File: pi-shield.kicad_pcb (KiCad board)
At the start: 2 copper layers, 65 x 56 mm, 34 parts, among them J1 Conn_02x20_Odd_Even, J10 Conn_01x04, J2 Conn_01x04, J3 Conn_01x04, J4 0530470210, J5 Conn_01x05, J6 Conn_01x07, J7 0530471410, J8 Conn_01x04, J9 Conn_01x04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

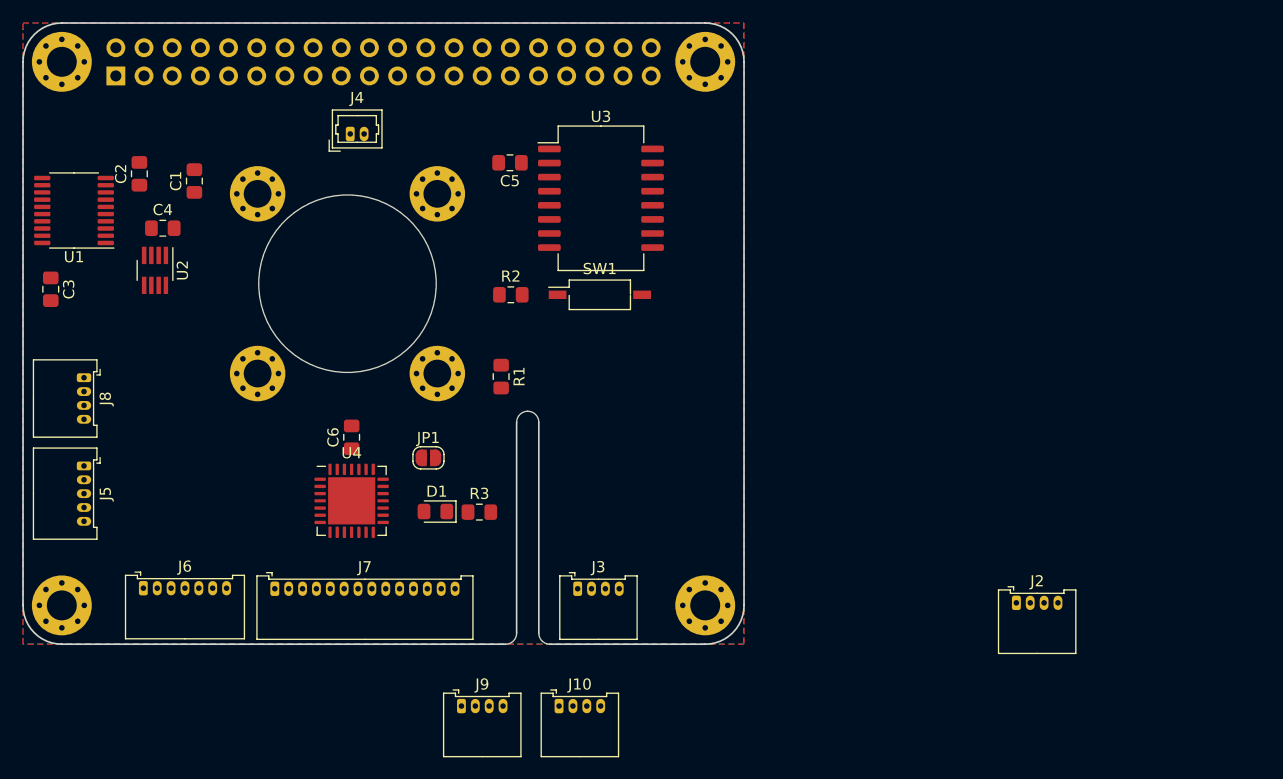
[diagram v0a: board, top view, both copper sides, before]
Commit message: Progress on schematic and board outline
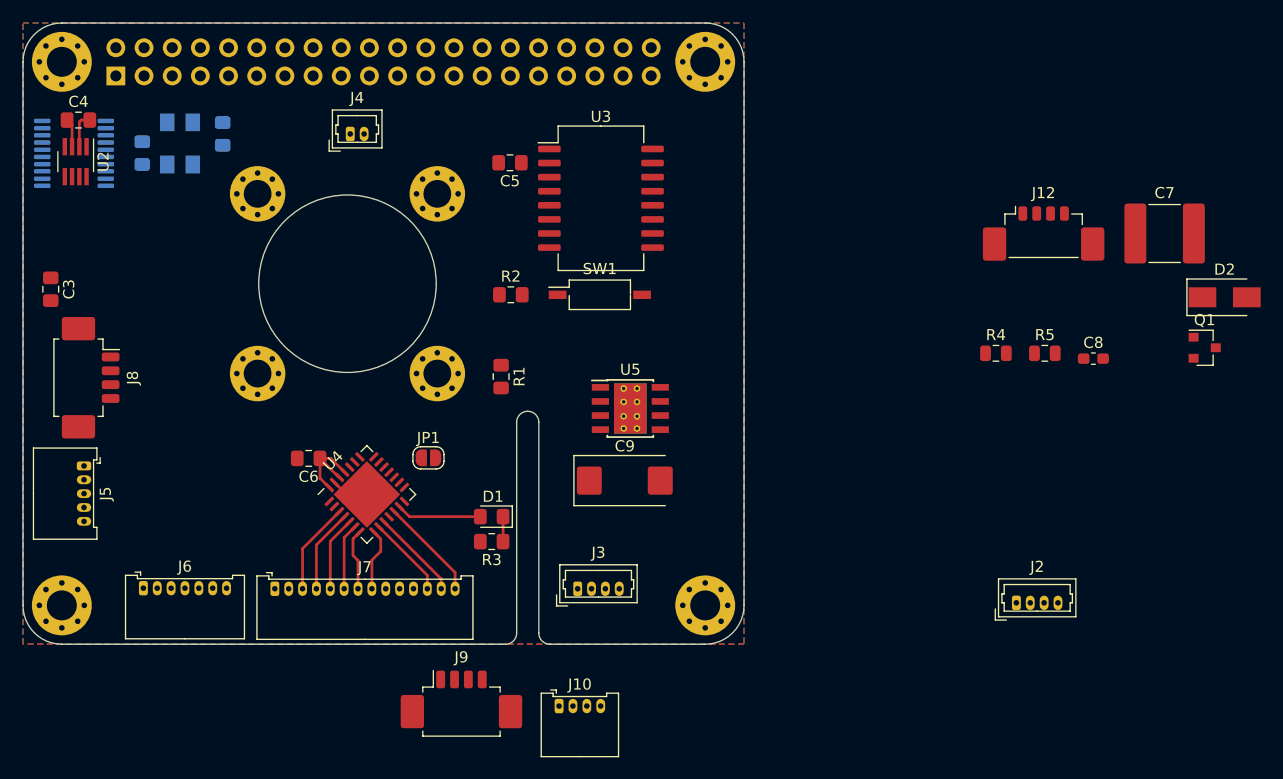
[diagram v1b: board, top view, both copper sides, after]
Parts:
- added C7: 10u, Capacitor_SMD:C_2220_5650Metric_Pad1.97x5.40mm_HandSolder, F.Cu at (139.4, 55.5)
- added C8: 10n, Capacitor_SMD:C_0603_1608Metric_Pad1.05x0.95mm_HandSolder, F.Cu at (133.0, 66.8)
- added C9: 330u, Capacitor_Tantalum_SMD:CP_EIA-7343-30_AVX-N_Pad2.25x2.55mm_HandSolder, F.Cu at (90.8, 77.8)
- added D2: B340A, Diode_SMD:D_SMA, F.Cu at (144.8, 61.2)
- added J12: Conn_01x03, Connector_Molex:Molex_PicoBlade_53398-0471_1x04-1MP_P1.25mm_Vertical, F.Cu at (128.5, 54.9)
- added Q1: DMP3099L, Package_TO_SOT_SMD:SOT-23, F.Cu at (143.0, 65.8)
- added R4: 10k, Resistor_SMD:R_0805_2012Metric, F.Cu at (124.2, 66.3)
- added R5: 3k24, Resistor_SMD:R_0805_2012Metric, F.Cu at (128.6, 66.3)
- added U5: TPS5430DDA, Package_SO:TI_SO-PowerPAD-8_ThermalVias, F.Cu at (91.2, 71.2)
- added Y1: 20Mhz, Crystal:Crystal_SMD_Abracon_ABM3C-4Pin_5.0x3.2mm, B.Cu at (50.6, 47.4)
- C1, C2, U1: moved to B.Cu
- J2, J3: footprint Connector_Molex:Molex_PicoBlade_53048-0410_1x04_P1.25mm_Horizontal -> Connector_Molex:Molex_PicoBlade_53047-0410_1x04_P1.25mm_Vertical
- J8, J9: footprint Connector_Molex:Molex_PicoBlade_53048-0410_1x04_P1.25mm_Horizontal -> Connector_Molex:Molex_PicoBlade_53261-0471_1x04-1MP_P1.25mm_Horizontal
- moved C4 12.4 mm to (41.5, 45.2)
- moved U2 12.1 mm to (41.2, 49.0)
- moved U1 5.15 mm to (41.1, 48.2)
- moved D1 5.10 mm to (78.8, 81.0)
- moved C1 4.95 mm to (54.5, 46.5), turned to 270 degrees
- moved C6 4.32 mm to (62.2, 75.8), turned to 180 degrees
- moved R3 2.88 mm to (78.8, 83.2), turned to 180 degrees
- moved C2 1.89 mm to (47.2, 48.2)
- moved U4 1.49 mm to (67.5, 79.0), turned to 45 degrees
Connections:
- J1 pad 1: Net-(J1-Pad1) -> +3V3
- J1 pad 36: Net-(J1-Pad36) -> /VBUS_DIS
- J1 pad 37: Net-(J1-Pad37) -> /CAN_INT
- U4 pad 13: Net-(U4-Pad13) -> /LED_BOARD
- U4 pad 16: /LED_BOARD -> Net-(U4-Pad16)
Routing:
- net +3V3: track 0.00 -> 10.8 mm
- net /LED_RGB_B: track 0.00 -> 9.22 mm
- net /LED_READY: track 0.00 -> 8.33 mm
- net /LED_RGB_G: track 0.00 -> 8.17 mm
- net /LED_BOARD: track 0.00 -> 7.68 mm
- net /LED_DEBUG: track 0.00 -> 7.55 mm
- net /LED_RGB_R: track 0.00 -> 7.38 mm
- net /LED_BUS: track 0.00 -> 6.76 mm
- net GND: track 0.00 -> 6.62 mm
- net /LED_COMM: track 0.00 -> 5.97 mm
- net /LED_POWER: track 0.00 -> 5.70 mm
- net /LED_ERROR: track 0.00 -> 5.56 mm
- net Net-(D1-Pad1): track 0.00 -> 2.25 mm

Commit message: Initial component placement
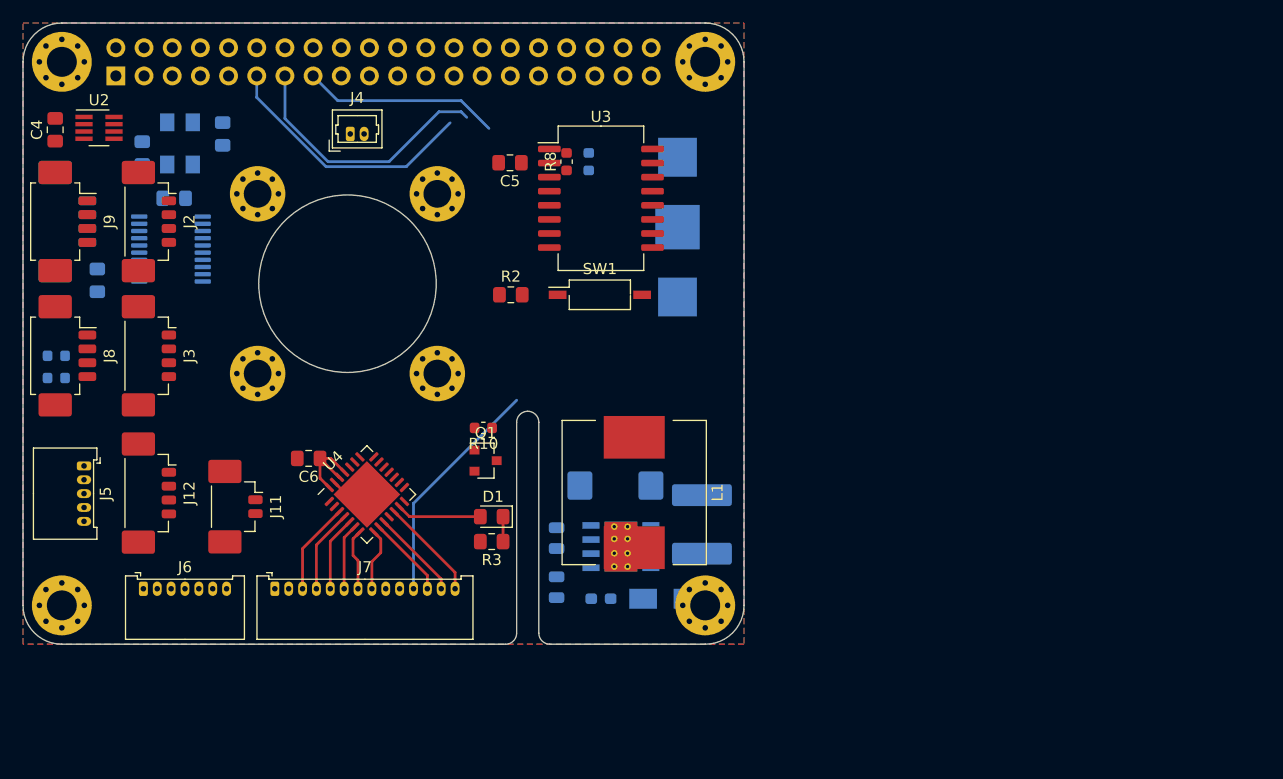
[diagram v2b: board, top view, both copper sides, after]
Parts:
- removed JP1: Jumper_NO_Small, Jumper:SolderJumper-2_P1.3mm_Open_RoundedPad1.0x1.5mm
- added BT1: 3V, pi-shield:3030, B.Cu at (95.5, 54.9)
- added J11: 0530470210, Connector_Molex:Molex_PicoBlade_53398-0271_1x02-1MP_P1.25mm_Vertical, F.Cu at (56.2, 80.1)
- added L1: 33uH, pi-shield:DR127, F.Cu at (91.6, 78.8)
- added R10: 10k, Resistor_SMD:R_0603_1608Metric, F.Cu at (78.0, 73.0)
- added R6: 100, Resistor_SMD:R_0603_1608Metric, B.Cu at (39.5, 66.5)
- added R7: 100, Resistor_SMD:R_0603_1608Metric, B.Cu at (39.5, 68.5)
- added R8: 1k, Resistor_SMD:R_0603_1608Metric, F.Cu at (85.5, 49.0)
- added R9: 1k, Resistor_SMD:R_0603_1608Metric, B.Cu at (87.5, 49.0)
- C3, C7, C8, C9, D2, R1, R4, R5, U5: moved to B.Cu
- J10: footprint Connector_Molex:Molex_PicoBlade_53048-0410_1x04_P1.25mm_Horizontal -> Connector_Molex:Molex_PicoBlade_53261-0471_1x04-1MP_P1.25mm_Horizontal; moved to B.Cu
- J2, J3: footprint Connector_Molex:Molex_PicoBlade_53047-0410_1x04_P1.25mm_Vertical -> Connector_Molex:Molex_PicoBlade_53398-0471_1x04-1MP_P1.25mm_Vertical
- moved J2 84.9 mm to (48.4, 54.4), turned to 270 degrees
- moved J12 83.6 mm to (48.4, 78.9), turned to 270 degrees
- moved Q1 65.6 mm to (78.2, 76.0)
- moved J10 62.7 mm to (39.9, 54.4), turned to 90 degrees
- moved D2 57.3 mm to (94.4, 88.4)
- moved J9 56.7 mm to (39.9, 54.4), turned to 270 degrees
- moved C8 49.4 mm to (88.6, 88.4), turned to 180 degrees
- moved C7 49.3 mm to (97.7, 81.7), turned to 90 degrees
- moved R5 48.8 mm to (84.6, 87.4), turned to 270 degrees
- moved J3 43.5 mm to (48.4, 66.5), turned to 270 degrees
- moved R4 43.0 mm to (84.6, 82.9), turned to 270 degrees
- moved R1 37.4 mm to (43.2, 59.7), turned to 90 degrees
- moved C3 13.8 mm to (50.1, 52.3), turned to 0 degrees
- moved U5 12.5 mm to (90.4, 83.7)
- moved U1 12.3 mm to (49.8, 56.9)
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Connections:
- J1 pad 10: /UART_RX -> Net-(J1-Pad10)
- J1 pad 32: Net-(J1-Pad32) -> /ROBOT_SELECT
- J1 pad 8: /UART_TX -> Net-(J1-Pad8)
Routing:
- net /BTN_START: track 0.00 -> 38.7 mm
- net /BTN_TEAM2: track 0.00 -> 23.9 mm
- net /BTN_TEAM1: track 0.00 -> 23.6 mm
- net GND: track 6.62 -> 3.38 mm
- net +3V3: track 10.8 -> 8.17 mm
- added copper zone on In1.Cu, net GND
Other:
- copper layers 2 -> 4

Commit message: Made some progress with layout
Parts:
- R1, R2, R3: footprint Resistor_SMD:R_0805_2012Metric_Pad1.15x1.40mm_HandSolder -> Resistor_SMD:R_0603_1608Metric
- R4, R5: footprint Resistor_SMD:R_0805_2012Metric -> Resistor_SMD:R_0603_1608Metric; moved to F.Cu
- R8: moved to B.Cu
- moved C1 28.6 mm to (43.8, 73.0), turned to 180 degrees
- moved Y1 26.6 mm to (48.5, 73.8), turned to 90 degrees
- moved C2 25.3 mm to (52.2, 73.0), turned to 270 degrees
- moved J4 24.8 mm to (80.6, 66.5), turned to 90 degrees
- moved C3 11.8 mm to (44.2, 62.5), turned to 90 degrees
- moved U1 9.64 mm to (49.2, 66.5)
- moved C4 7.31 mm to (46.7, 45.7), turned to 270 degrees
- moved R1 5.96 mm to (42.9, 65.7), turned to 0 degrees
- moved R8 4.34 mm to (88.9, 51.7), turned to 180 degrees
- moved D2 4.30 mm to (90.1, 88.5), turned to 180 degrees
- moved C8 4.28 mm to (84.4, 87.6), turned to 90 degrees
- moved R5 4.07 mm to (84.3, 83.3)
- moved R7 3.61 mm to (39.8, 64.9), turned to 90 degrees
- moved R4 3.40 mm to (84.3, 79.5)
- moved R6 2.03 mm to (38.2, 64.9), turned to 90 degrees
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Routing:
- net /TS_INT: track 0.00 -> 131.2 mm
- net +5V: track 0.00 -> 127.6 mm, vias 0 -> 4
- net /SDA: track 0.00 -> 119.9 mm, vias 0 -> 4
- net /SCL: track 0.00 -> 115.6 mm, vias 0 -> 3
- net /SCLK: track 0.00 -> 76.3 mm, vias 0 -> 1
- net +12V: track 0.00 -> 74.2 mm, vias 0 -> 2
- net /MOSI: track 0.00 -> 70.4 mm, vias 0 -> 2
- net /SHDN_OK: track 0.00 -> 69.9 mm, vias 0 -> 2
- net /CS1: track 0.00 -> 68.5 mm
- net /SHDN_REQ: track 0.00 -> 67.2 mm, vias 0 -> 2
- net /CAN_INT: track 0.00 -> 65.1 mm
- net /LCD_RST: track 0.00 -> 64.9 mm, vias 0 -> 2
- net /LCD_RS: track 0.00 -> 58.8 mm, vias 0 -> 2
- net /CS0: track 0.00 -> 46.7 mm, vias 0 -> 1
- net /CANL: track 0.00 -> 45.4 mm, vias 0 -> 1
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- added copper zone on In2.Cu, net +3V3
- added copper zone on B.Cu, net +5V
- added copper zone on F.Cu, net +5V

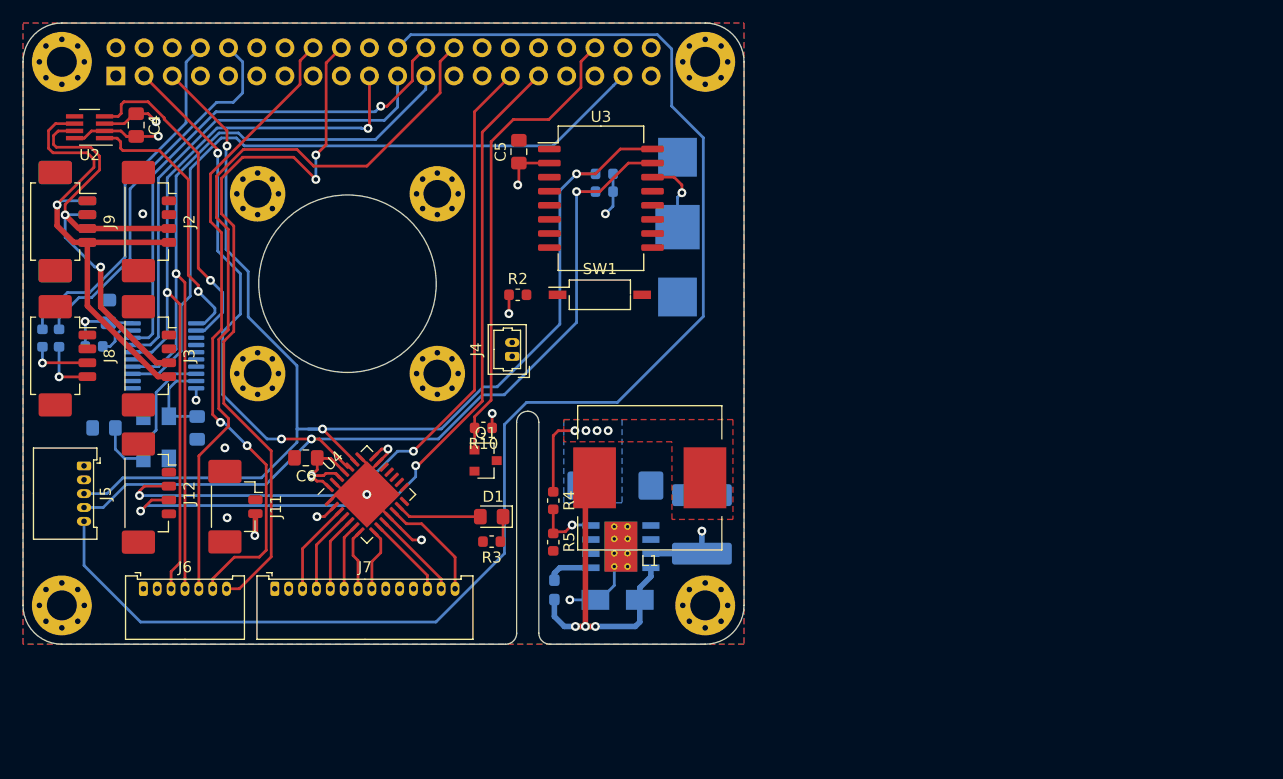
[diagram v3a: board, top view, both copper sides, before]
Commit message: First complete layout
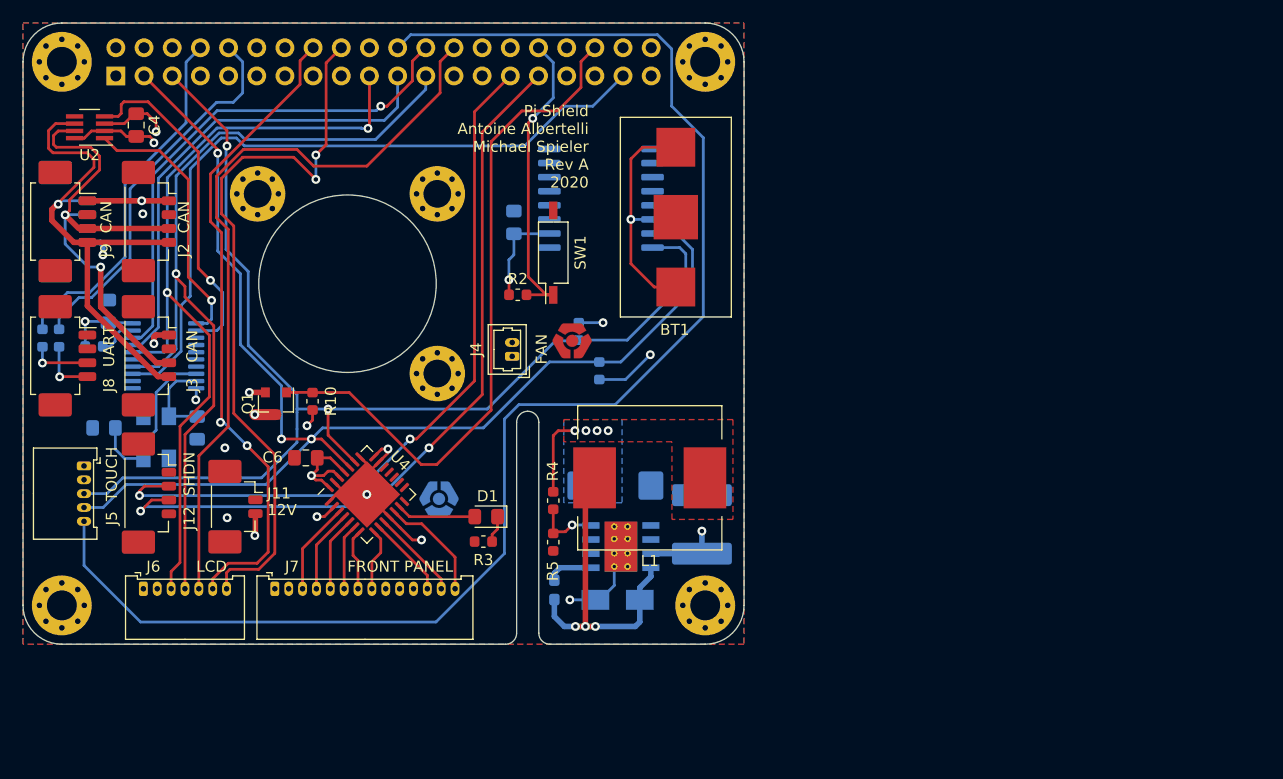
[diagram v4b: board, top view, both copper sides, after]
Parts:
- removed H4: M2, MountingHole:MountingHole_2.5mm_Pad_Via
- added G***: LOGO, pi-shield:CVRA-logo-small-copper, B.Cu at (74.0, 79.4)
- added G***: LOGO, pi-shield:CVRA-logo-small-copper, F.Cu at (86.0, 65.2)
- BT1: moved to F.Cu
- C5, U3: moved to B.Cu
- moved Q1 19.6 mm to (59.3, 70.8), turned to 270 degrees
- moved R8 16.2 mm to (88.5, 67.8), turned to 90 degrees
- moved R10 15.6 mm to (62.6, 70.6), turned to 90 degrees
- moved R9 14.4 mm to (86.6, 64.3), turned to 270 degrees
- moved C5 6.39 mm to (80.8, 54.5)
- moved SW1 5.66 mm to (84.3, 57.2), turned to 90 degrees
- moved BT1 0.91 mm to (95.3, 54.0)
- moved R3 0.75 mm to (78.0, 83.2)
- moved D1 0.50 mm to (78.2, 81.0)
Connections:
- J1 pad 11: /BTN_TEAM1 -> /BTN_START
- J1 pad 15: /BTN_START -> /BTN_TEAM1
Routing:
- net /BTN_START: track 0.00 -> 100.7 mm
- net /BTN_TEAM2: track 0.00 -> 99.7 mm
- net /BTN_TEAM1: track 0.00 -> 98.7 mm
- net VBUS: track 0.00 -> 43.6 mm, vias 0 -> 4
- net /ROBOT_SELECT: track 0.00 -> 27.5 mm, vias 0 -> 1
- net /VBUS_DIS: track 42.6 -> 61.6 mm
- net +5V: track 127.6 -> 141.6 mm, vias 4 -> 5
- net +BATT: track 6.91 -> 20.8 mm
- net +3V3: track 35.2 -> 42.8 mm
- net /SCL: track 115.6 -> 110.2 mm, vias 3 -> 2
- net /SDA: track 119.9 -> 115.9 mm, vias 4 -> 3
- net /MOSI: track 70.4 -> 73.1 mm
- net /SCLK: track 76.3 -> 78.5 mm
- net /SHDN_OK: track 69.9 -> 68.9 mm
- net /CS1: track 68.5 -> 67.8 mm
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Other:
- net class Default: clearance 0.2 -> 0.15
- rule trace_clearance: 0.2 -> 0.15
- board text added: "12V"
- board text added: "CAN"
- board text added: "FAN"
- board text added: "FRONT PANEL"
- board text added: "LCD"
- board text added: "Layer setup F.Cu: Top In1.Cu: GND In2.Cu: 3.3V B.Cu: Bottom"
- board text added: "Pi Shield Antoine Albertelli Michael Spieler Rev A 2020"
- board text added: "SHDN"
- board text added: "TOUCH"
- board text added: "UART"
